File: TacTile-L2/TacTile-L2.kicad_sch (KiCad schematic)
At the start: 11 parts, among them J1 Conn_01x05, J2 Conn_01x05, U1 74HC595

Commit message: Added some footprints for laser boards
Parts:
- J1: footprint (none) -> Connector_PinHeader_2.00mm:PinHeader_1x05_P2.00mm_Horizontal
- J2: footprint (none) -> Connector_PinSocket_2.00mm:PinSocket_1x05_P2.00mm_Horizontal
- U1: footprint (none) -> Package_DIP:DIP-16_W7.62mm
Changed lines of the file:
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@@
       (effects (font (size 1.27 1.27)))
     )
-    (property "Footprint" "" (at 34.29 48.26 0)
+    (property "Footprint" "Connector_PinSocket_2.00mm:PinSocket_1x05_P2.00mm_Horizontal" (at 34.29 48.26 0)
       (effects (font (size 1.27 1.27)) hide)
     )
@@
       (effects (font (size 1.27 1.27)))
     )
-    (property "Footprint" "" (at 34.29 22.86 0)
+    (property "Footprint" "Connector_PinHeader_2.00mm:PinHeader_1x05_P2.00mm_Horizontal" (at 34.29 22.86 0)
       (effects (font (size 1.27 1.27)) hide)
     )
@@
       (effects (font (size 1.27 1.27)) (justify left))
     )
-    (property "Footprint" "" (at 55.88 34.29 0)
-      (effects (font (size 1.27 1.27)) hide)
-    )
+    (property "Footprint" "Package_DIP:DIP-16_W7.62mm" (at 55.88 34.29 0)
+      (effects (font (size 1.27 1.27)) hide)
+    )

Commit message: Added photoresistor footprint and enlarged main boards to 60mm
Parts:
- R1, R2, R3, R4, R5, R6, R7, R8: footprint (none) -> TacTile:Photoresistor
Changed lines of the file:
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@@
       (effects (font (size 1.27 1.27)) (justify left top))
     )
-    (property "Footprint" "" (at 72.39 69.85 90)
+    (property "Footprint" "TacTile:Photoresistor" (at 72.39 69.85 90)
       (effects (font (size 1.27 1.27)) (justify left) hide)
     )
@@
       (effects (font (size 1.27 1.27)) (justify left top))
     )
-    (property "Footprint" "" (at 72.39 44.45 90)
+    (property "Footprint" "TacTile:Photoresistor" (at 72.39 44.45 90)
       (effects (font (size 1.27 1.27)) (justify left) hide)
     )
@@
       (effects (font (size 1.27 1.27)))
     )
-    (property "Footprint" "" (at 72.39 25.4 90)
+    (property "Footprint" "TacTile:Photoresistor" (at 72.39 25.4 90)
       (effects (font (size 1.27 1.27)) (justify left) hide)
     )
@@
       (effects (font (size 1.27 1.27)) (justify left top))
     )
-    (property "Footprint" "" (at 72.39 38.1 90)
+    (property "Footprint" "TacTile:Photoresistor" (at 72.39 38.1 90)
       (effects (font (size 1.27 1.27)) (justify left) hide)
     )
@@
       (effects (font (size 1.27 1.27)) (justify left top))
     )
-    (property "Footprint" "" (at 72.39 63.5 90)
+    (property "Footprint" "TacTile:Photoresistor" (at 72.39 63.5 90)
       (effects (font (size 1.27 1.27)) (justify left) hide)
     )
@@
       (effects (font (size 1.27 1.27)) (justify left top))
     )
-    (property "Footprint" "" (at 72.39 31.75 90)
+    (property "Footprint" "TacTile:Photoresistor" (at 72.39 31.75 90)
       (effects (font (size 1.27 1.27)) (justify left) hide)
     )
@@
       (effects (font (size 1.27 1.27)) (justify left top))
     )
-    (property "Footprint" "" (at 72.39 57.15 90)
+    (property "Footprint" "TacTile:Photoresistor" (at 72.39 57.15 90)
       (effects (font (size 1.27 1.27)) (justify left) hide)
     )
@@
       (effects (font (size 1.27 1.27)) (justify left top))
     )
-    (property "Footprint" "" (at 72.39 50.8 90)
-      (effects (font (size 1.27 1.27)) (justify left) hide)
-    )
+    (property "Footprint" "TacTile:Photoresistor" (at 72.39 50.8 90)
+      (effects (font (size 1.27 1.27)) (justify left) hide)
+    )

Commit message: Finished L2 Board
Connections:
- net GND: now also J2.2 (Pin_2); no longer J2.4 (Pin_4)
- net OUT: now also J2.5 (Pin_5); no longer J2.1 (Pin_1)
- net SOUT: now also J2.4 (Pin_4); no longer J2.2 (Pin_2)
- net VCC: now also J2.1 (Pin_1); no longer J2.5 (Pin_5)
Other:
- moved on the sheet: J2
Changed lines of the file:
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@@
   (junction (at 82.55 49.53) (diameter 0) (color 0 0 0 0)
   )
-  (junction (at 39.37 43.18) (diameter 0) (color 0 0 0 0)
-  )
   (junction (at 31.75 41.91) (diameter 0) (color 0 0 0 0)
   )
@@
   (junction (at 82.55 36.83) (diameter 0) (color 0 0 0 0)
   )
+  (junction (at 39.37 50.8) (diameter 0) (color 0 0 0 0)
+  )
   (wire (pts (xy 55.88 19.05) (xy 55.88 15.24))
     (stroke (width 0) (type default))
   )
-  (wire (pts (xy 36.83 40.64) (xy 36.83 43.18))
-    (stroke (width 0) (type default))
-  )
   (wire (pts (xy 82.55 24.13) (xy 82.55 30.48))
     (stroke (width 0) (type default))
@@
     (stroke (width 0) (type default))
   )
+  (wire (pts (xy 34.29 27.94) (xy 34.29 36.83))
+    (stroke (width 0) (type default))
+  )
   (wire (pts (xy 45.72 39.37) (xy 55.88 39.37))
     (stroke (width 0) (type default))
   )
-  (wire (pts (xy 45.72 55.88) (xy 45.72 40.64))
+  (wire (pts (xy 46.99 55.88) (xy 46.99 52.07))
     (stroke (width 0) (type default))
   )
@@
     (stroke (width 0) (type default))
   )
-  (wire (pts (xy 43.18 43.18) (xy 43.18 72.39))
+  (wire (pts (xy 43.18 50.8) (xy 43.18 72.39))
     (stroke (width 0) (type default))
   )
@@
     (stroke (width 0) (type default))
   )
+  (wire (pts (xy 31.75 41.91) (xy 31.75 50.8))
+    (stroke (width 0) (type default))
+  )
   (wire (pts (xy 73.66 36.83) (xy 74.93 36.83))
     (stroke (width 0) (type default))
@@
     (stroke (width 0) (type default))
   )
-  (wire (pts (xy 45.72 40.64) (xy 36.83 40.64))
-    (stroke (width 0) (type default))
-  )
   (wire (pts (xy 45.72 29.21) (xy 44.45 29.21))
     (stroke (width 0) (type default))
   )
-  (wire (pts (xy 29.21 27.94) (xy 29.21 43.18))
-    (stroke (width 0) (type default))
-  )
   (wire (pts (xy 82.55 49.53) (xy 82.55 55.88))
     (stroke (width 0) (type default))
   )
-  (wire (pts (xy 34.29 36.83) (xy 34.29 43.18))
-    (stroke (width 0) (type default))
-  )
   (wire (pts (xy 82.55 55.88) (xy 82.55 62.23))
     (stroke (width 0) (type default))
   )
+  (wire (pts (xy 36.83 52.07) (xy 46.99 52.07))
+    (stroke (width 0) (type default))
+  )
   (wire (pts (xy 36.83 30.48) (xy 36.83 27.94))
     (stroke (width 0) (type default))
@@
     (stroke (width 0) (type default))
   )
-  (wire (pts (xy 39.37 27.94) (xy 39.37 43.18))
+  (wire (pts (xy 39.37 27.94) (xy 39.37 50.8))
     (stroke (width 0) (type default))
   )
@@
     (stroke (width 0) (type default))
   )
+  (wire (pts (xy 29.21 27.94) (xy 29.21 50.8))
+    (stroke (width 0) (type default))
+  )
   (wire (pts (xy 66.04 29.21) (xy 73.66 29.21))
     (stroke (width 0) (type default))
@@
     (stroke (width 0) (type default))
   )
-  (wire (pts (xy 66.04 55.88) (xy 45.72 55.88))
+  (wire (pts (xy 66.04 55.88) (xy 46.99 55.88))
     (stroke (width 0) (type default))
   )
@@
     (stroke (width 0) (type default))
   )
+  (wire (pts (xy 36.83 52.07) (xy 36.83 50.8))
+    (stroke (width 0) (type default))
+  )
   (wire (pts (xy 55.88 54.61) (xy 26.67 54.61))
     (stroke (width 0) (type default))
@@
     (stroke (width 0) (type default))
   )
-  (wire (pts (xy 31.75 41.91) (xy 31.75 43.18))
-    (stroke (width 0) (type default))
-  )
   (wire (pts (xy 66.04 39.37) (xy 68.58 39.37))
     (stroke (width 0) (type default))
@@
     (stroke (width 0) (type default))
   )
+  (wire (pts (xy 34.29 36.83) (xy 34.29 50.8))
+    (stroke (width 0) (type default))
+  )
   (wire (pts (xy 68.58 62.23) (xy 74.93 62.23))
     (stroke (width 0) (type default))
@@
     (stroke (width 0) (type default))
   )
-  (wire (pts (xy 34.29 36.83) (xy 34.29 27.94))
-    (stroke (width 0) (type default))
-  )
   (wire (pts (xy 67.31 41.91) (xy 67.31 68.58))
     (stroke (width 0) (type default))
@@
     (stroke (width 0) (type default))
   )
-  (wire (pts (xy 39.37 43.18) (xy 43.18 43.18))
+  (wire (pts (xy 39.37 50.8) (xy 43.18 50.8))
     (stroke (width 0) (type default))
   )
@@
     (effects (font (size 1.27 1.27)) (justify left bottom))
   )
-  (label "CLK" (at 34.29 36.83 0) (fields_autoplaced)
-    (effects (font (size 1.27 1.27)) (justify left bottom))
-  )
-  (symbol (lib_id "Connector_Generic:Conn_01x05") (at 34.29 48.26 270) (unit 1)
+  (label "CLK" (at 34.29 34.29 0) (fields_autoplaced)
+    (effects (font (size 1.27 1.27)) (justify left bottom))
+  )
+  (symbol (lib_id "Connector_Generic:Conn_01x05") (at 34.29 45.72 90) (unit 1)
     (in_bom yes) (on_board yes) (dnp no)
-    (property "Reference" "J2" (at 34.29 53.34 90)
+    (property "Reference" "J2" (at 34.29 40.64 90)
       (effects (font (size 1.27 1.27)))
     )
-    (property "Value" "Conn_01x05" (at 34.29 50.8 90)
+    (property "Value" "Conn_01x05" (at 34.29 43.18 90)
       (effects (font (size 1.27 1.27)))
     )
-    (property "Footprint" "Connector_PinSocket_2.00mm:PinSocket_1x05_P2.00mm_Horizontal" (at 34.29 48.26 0)
+    (property "Footprint" "Connector_PinSocket_2.00mm:PinSocket_1x05_P2.00mm_Horizontal" (at 34.29 45.72 0)
       (effects (font (size 1.27 1.27)) hide)
     )
-    (property "Datasheet" "~" (at 34.29 48.26 0)
+    (property "Datasheet" "~" (at 34.29 45.72 0)
       (effects (font (size 1.27 1.27)) hide)
     )

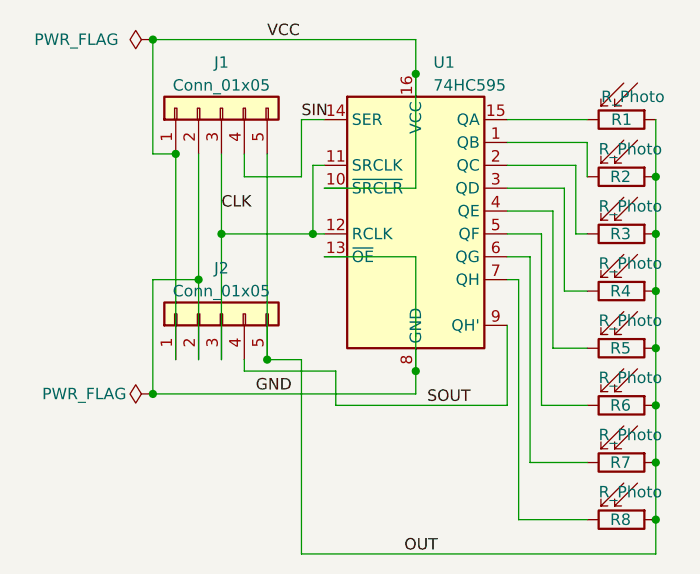
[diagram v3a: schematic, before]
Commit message: Finished enlarging pins on C, D, L1, L2
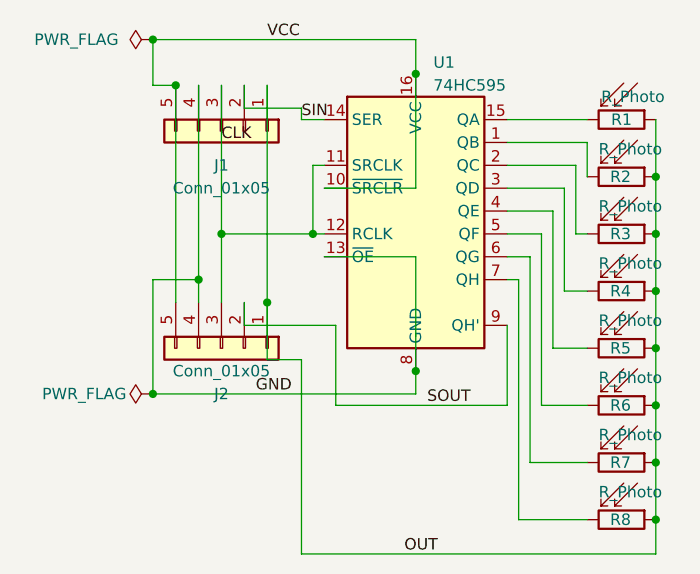
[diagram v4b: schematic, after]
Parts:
- J1: footprint Connector_PinHeader_2.00mm:PinHeader_1x05_P2.00mm_Horizontal -> Connector_PinSocket_2.54mm:PinSocket_1x05_P2.54mm_Horizontal
- J2: footprint Connector_PinSocket_2.00mm:PinSocket_1x05_P2.00mm_Horizontal -> Connector_PinHeader_2.54mm:PinHeader_1x05_P2.54mm_Horizontal
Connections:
- net GND: now also J1.4 (Pin_4), J2.4 (Pin_4); no longer J1.2 (Pin_2), J2.2 (Pin_2)
- net OUT: now also J1.1 (Pin_1), J2.1 (Pin_1); no longer J1.5 (Pin_5), J2.5 (Pin_5)
- net SIN: now also J1.2 (Pin_2); no longer J1.4 (Pin_4)
- net SOUT: now also J2.2 (Pin_2); no longer J2.4 (Pin_4)
- net VCC: now also J1.5 (Pin_5), J2.5 (Pin_5); no longer J1.1 (Pin_1), J2.1 (Pin_1)
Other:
- moved on the sheet: J1, J2
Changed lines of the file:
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@@
 (kicad_sch (version 20230121) (generator eeschema)
   (paper "A4")
-  (junction (at 29.21 27.94) (diameter 0) (color 0 0 0 0)
-  )
   (junction (at 82.55 49.53) (diameter 0) (color 0 0 0 0)
   )
@@
   (junction (at 82.55 43.18) (diameter 0) (color 0 0 0 0)
   )
+  (junction (at 39.37 44.45) (diameter 0) (color 0 0 0 0)
+  )
   (junction (at 26.67 54.61) (diameter 0) (color 0 0 0 0)
   )
+  (junction (at 29.21 20.32) (diameter 0) (color 0 0 0 0)
+  )
   (junction (at 82.55 68.58) (diameter 0) (color 0 0 0 0)
   )
   (junction (at 82.55 36.83) (diameter 0) (color 0 0 0 0)
   )
-  (junction (at 39.37 50.8) (diameter 0) (color 0 0 0 0)
-  )
   (wire (pts (xy 55.88 19.05) (xy 55.88 15.24))
     (stroke (width 0) (type default))
   )
+  (wire (pts (xy 31.75 20.32) (xy 31.75 41.91))
+    (stroke (width 0) (type default))
+  )
   (wire (pts (xy 82.55 24.13) (xy 82.55 30.48))
     (stroke (width 0) (type default))
@@
     (stroke (width 0) (type default))
   )
-  (wire (pts (xy 34.29 27.94) (xy 34.29 36.83))
-    (stroke (width 0) (type default))
-  )
   (wire (pts (xy 45.72 39.37) (xy 55.88 39.37))
     (stroke (width 0) (type default))
   )
-  (wire (pts (xy 46.99 55.88) (xy 46.99 52.07))
+  (wire (pts (xy 46.99 55.88) (xy 46.99 46.99))
     (stroke (width 0) (type default))
   )
@@
     (stroke (width 0) (type default))
   )
-  (wire (pts (xy 26.67 15.24) (xy 26.67 27.94))
+  (wire (pts (xy 26.67 15.24) (xy 26.67 20.32))
     (stroke (width 0) (type default))
   )
@@
     (stroke (width 0) (type default))
   )
-  (wire (pts (xy 31.75 41.91) (xy 31.75 50.8))
+  (wire (pts (xy 31.75 41.91) (xy 31.75 44.45))
     (stroke (width 0) (type default))
   )
@@
     (stroke (width 0) (type default))
   )
+  (wire (pts (xy 39.37 20.32) (xy 39.37 44.45))
+    (stroke (width 0) (type default))
+  )
   (wire (pts (xy 66.04 34.29) (xy 71.12 34.29))
     (stroke (width 0) (type default))
@@
     (stroke (width 0) (type default))
   )
-  (wire (pts (xy 36.83 52.07) (xy 46.99 52.07))
-    (stroke (width 0) (type default))
-  )
-  (wire (pts (xy 36.83 30.48) (xy 36.83 27.94))
+  (wire (pts (xy 36.83 46.99) (xy 46.99 46.99))
+    (stroke (width 0) (type default))
+  )
+  (wire (pts (xy 36.83 22.86) (xy 36.83 20.32))
     (stroke (width 0) (type default))
   )
@@
     (stroke (width 0) (type default))
   )
-  (wire (pts (xy 39.37 27.94) (xy 39.37 50.8))
-    (stroke (width 0) (type default))
-  )
   (wire (pts (xy 55.88 39.37) (xy 55.88 52.07))
     (stroke (width 0) (type default))
@@
     (stroke (width 0) (type default))
   )
-  (wire (pts (xy 43.18 24.13) (xy 43.18 30.48))
+  (wire (pts (xy 43.18 22.86) (xy 43.18 24.13))
     (stroke (width 0) (type default))
   )
@@
     (stroke (width 0) (type default))
   )
-  (wire (pts (xy 29.21 27.94) (xy 29.21 50.8))
+  (wire (pts (xy 29.21 20.32) (xy 29.21 44.45))
     (stroke (width 0) (type default))
   )
@@
     (stroke (width 0) (type default))
   )
-  (wire (pts (xy 36.83 52.07) (xy 36.83 50.8))
+  (wire (pts (xy 36.83 46.99) (xy 36.83 44.45))
     (stroke (width 0) (type default))
   )
@@
     (stroke (width 0) (type default))
   )
+  (wire (pts (xy 34.29 20.32) (xy 34.29 36.83))
+    (stroke (width 0) (type default))
+  )
   (wire (pts (xy 66.04 24.13) (xy 74.93 24.13))
     (stroke (width 0) (type default))
@@
     (stroke (width 0) (type default))
   )
-  (wire (pts (xy 34.29 36.83) (xy 34.29 50.8))
+  (wire (pts (xy 34.29 36.83) (xy 34.29 44.45))
     (stroke (width 0) (type default))
   )
@@
     (stroke (width 0) (type default))
   )
-  (wire (pts (xy 26.67 27.94) (xy 29.21 27.94))
+  (wire (pts (xy 26.67 20.32) (xy 29.21 20.32))
     (stroke (width 0) (type default))
   )
@@
     (stroke (width 0) (type default))
   )
-  (wire (pts (xy 31.75 27.94) (xy 31.75 41.91))
-    (stroke (width 0) (type default))
-  )
-  (wire (pts (xy 43.18 30.48) (xy 36.83 30.48))
+  (wire (pts (xy 43.18 22.86) (xy 36.83 22.86))
+    (stroke (width 0) (type default))
+  )
+  (wire (pts (xy 39.37 44.45) (xy 39.37 50.8))
     (stroke (width 0) (type default))
   )
@@
     (effects (font (size 1.27 1.27)) (justify left bottom))
   )
-  (label "CLK" (at 34.29 34.29 0) (fields_autoplaced)
-    (effects (font (size 1.27 1.27)) (justify left bottom))
-  )
-  (symbol (lib_id "Connector_Generic:Conn_01x05") (at 34.29 45.72 90) (unit 1)
-    (in_bom yes) (on_board yes) (dnp no)
-    (property "Reference" "J2" (at 34.29 40.64 90)
-      (effects (font (size 1.27 1.27)))
-    )
-    (property "Value" "Conn_01x05" (at 34.29 43.18 90)
-      (effects (font (size 1.27 1.27)))
-    )
-    (property "Footprint" "Connector_PinSocket_2.00mm:PinSocket_1x05_P2.00mm_Horizontal" (at 34.29 45.72 0)
-      (effects (font (size 1.27 1.27)) hide)
-    )
-    (property "Datasheet" "~" (at 34.29 45.72 0)
+  (label "CLK" (at 34.29 26.67 0) (fields_autoplaced)
+    (effects (font (size 1.27 1.27)) (justify left bottom))
+  )
+  (symbol (lib_id "Connector_Generic:Conn_01x05") (at 34.29 49.53 270) (unit 1)
+    (in_bom yes) (on_board yes) (dnp no)
+    (property "Reference" "J2" (at 34.29 54.61 90)
+      (effects (font (size 1.27 1.27)))
+    )
+    (property "Value" "Conn_01x05" (at 34.29 52.07 90)
+      (effects (font (size 1.27 1.27)))
+    )
+    (property "Footprint" "Connector_PinHeader_2.54mm:PinHeader_1x05_P2.54mm_Horizontal" (at 34.29 49.53 0)
+      (effects (font (size 1.27 1.27)) hide)
+    )
+    (property "Datasheet" "~" (at 34.29 49.53 0)
       (effects (font (size 1.27 1.27)) hide)
     )
@@
     )
   )
-  (symbol (lib_id "Connector_Generic:Conn_01x05") (at 34.29 22.86 90) (unit 1)
+  (symbol (lib_id "Connector_Generic:Conn_01x05") (at 34.29 25.4 270) (unit 1)
     (in_bom yes) (on_board yes) (dnp no) (fields_autoplaced)
-    (property "Reference" "J1" (at 34.29 17.78 90)
-      (effects (font (size 1.27 1.27)))
-    )
-    (property "Value" "Conn_01x05" (at 34.29 20.32 90)
-      (effects (font (size 1.27 1.27)))
-    )
-    (property "Footprint" "Connector_PinHeader_2.00mm:PinHeader_1x05_P2.00mm_Horizontal" (at 34.29 22.86 0)
-      (effects (font (size 1.27 1.27)) hide)
-    )
-    (property "Datasheet" "~" (at 34.29 22.86 0)
-      (effects (font (size 1.27 1.27)) hide)
-    )
+    (property "Reference" "J1" (at 34.29 29.21 90)
+      (effects (font (size 1.27 1.27)))
+    )
+    (property "Value" "Conn_01x05" (at 34.29 31.75 90)
+      (effects (font (size 1.27 1.27)))
+    )
+    (property "Footprint" "Connector_PinSocket_2.54mm:PinSocket_1x05_P2.54mm_Horizontal" (at 34.29 25.4 0)
+      (effects (font (size 1.27 1.27)) hide)
+    )
+    (property "Datasheet" "~" (at 34.29 25.4 0)
+      (effects (font (size 1.27 1.27)) hide)
+    )
